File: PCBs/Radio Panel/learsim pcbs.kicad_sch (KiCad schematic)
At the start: 58 parts, among them SW1 MHz, SW2 KHz, SW3 2MD1T1B1M2QES-5, U1 ESP32-C6-DEV-KIT-N8, U2 MAX7219, U3 MAX7219

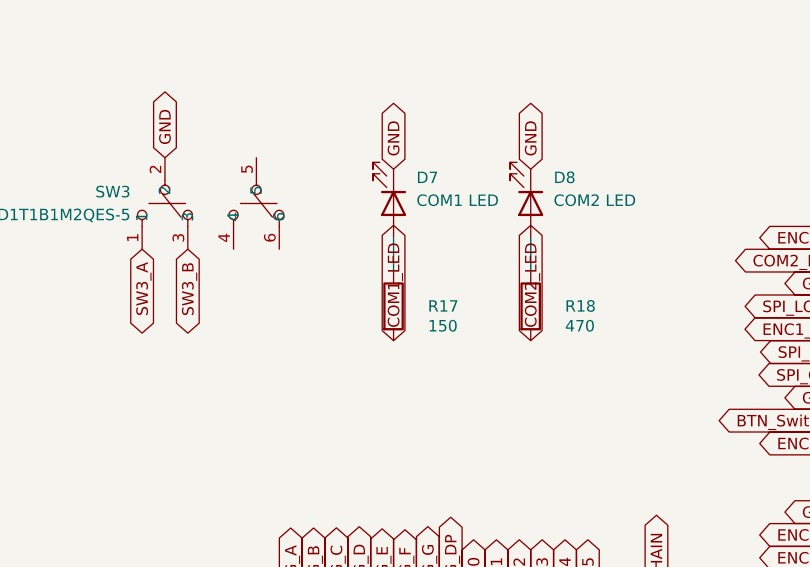
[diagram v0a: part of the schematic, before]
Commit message: Add new drill files and job configuration for learsim PCBs
- Created non-plated through hole (NPTH) drill file for learsim PCBs.
- Created plated through hole (PTH) drill file for learsim PCBs.
- Added job configuration file for learsim PCBs including specifications and file attributes.
- Updated symbol library table to include new components for the project.
- Modified project settings in .kicad_prl file to adjust active layer and visibility settings.
- Updated project properties in .kicad_pro file to include step file path and cleaned up used designators.
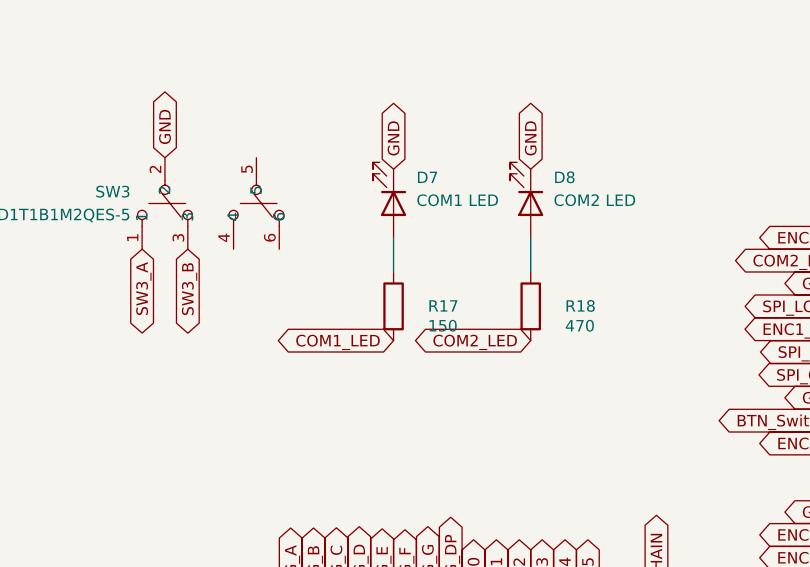
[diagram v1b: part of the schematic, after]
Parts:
- ADF1, COM1, COM2, NAV1, NAV2, Switch1: footprint PCM_Switch_Keyboard_Cherry_MX:SW_Cherry_MX_PCB -> PCM_Switch_Keyboard_Kailh:SW_Kailh_Choc_V2
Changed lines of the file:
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@@
 	(global_label "COM2_LED"
 		(shape bidirectional)
-		(at 76.2 92.71 90)
+		(at 76.2 92.71 180)
 		(fields_autoplaced yes)
 		(effects
@@
 				(size 1.27 1.27)
 			)
-			(justify left)
+			(justify right)
 		)
 		(property "Intersheetrefs" "${INTERSHEET_REFS}"
-			(at 84.2 92.71 0)
+			(at 62.4274 92.71 0)
 			(hide yes)
 			(show_name no)
@@
 					(size 1.27 1.27)
 				)
-				(justify left)
+				(justify right)
 			)
 		)
@@
 	(global_label "COM1_LED"
 		(shape bidirectional)
-		(at 60.96 92.71 90)
+		(at 60.96 92.71 180)
 		(fields_autoplaced yes)
 		(effects
@@
 				(size 1.27 1.27)
 			)
-			(justify left)
+			(justify right)
 		)
 		(property "Intersheetrefs" "${INTERSHEET_REFS}"
-			(at 68.96 92.71 0)
+			(at 47.1874 92.71 0)
 			(hide yes)
 			(show_name no)
@@
 					(size 1.27 1.27)
 				)
-				(justify left)
+				(justify right)
 			)
 		)
@@
 			)
 		)
-		(property "Footprint" "PCM_Switch_Keyboard_Cherry_MX:SW_Cherry_MX_PCB"
+		(property "Footprint" "PCM_Switch_Keyboard_Kailh:SW_Kailh_Choc_V2"
 			(at 161.29 52.07 0)
 			(hide yes)
@@
 			)
 		)
-		(property "Footprint" "PCM_Switch_Keyboard_Cherry_MX:SW_Cherry_MX_PCB"
+		(property "Footprint" "PCM_Switch_Keyboard_Kailh:SW_Kailh_Choc_V2"
 			(at 114.3 52.07 0)
 			(hide yes)
@@
 			)
 		)
-		(property "Footprint" "PCM_Switch_Keyboard_Cherry_MX:SW_Cherry_MX_PCB"
+		(property "Footprint" "PCM_Switch_Keyboard_Kailh:SW_Kailh_Choc_V2"
 			(at 144.78 52.07 0)
 			(hide yes)
@@
 			)
 		)
-		(property "Footprint" "PCM_Switch_Keyboard_Cherry_MX:SW_Cherry_MX_PCB"
+		(property "Footprint" "PCM_Switch_Keyboard_Kailh:SW_Kailh_Choc_V2"
 			(at 176.53 52.07 0)
 			(hide yes)
@@
 			)
 		)
-		(property "Footprint" "PCM_Switch_Keyboard_Cherry_MX:SW_Cherry_MX_PCB"
+		(property "Footprint" "PCM_Switch_Keyboard_Kailh:SW_Kailh_Choc_V2"
 			(at 191.77 52.07 0)
 			(hide yes)
@@
 			)
 		)
-		(property "Footprint" "PCM_Switch_Keyboard_Cherry_MX:SW_Cherry_MX_PCB"
+		(property "Footprint" "PCM_Switch_Keyboard_Kailh:SW_Kailh_Choc_V2"
 			(at 130.81 52.07 0)
 			(hide yes)

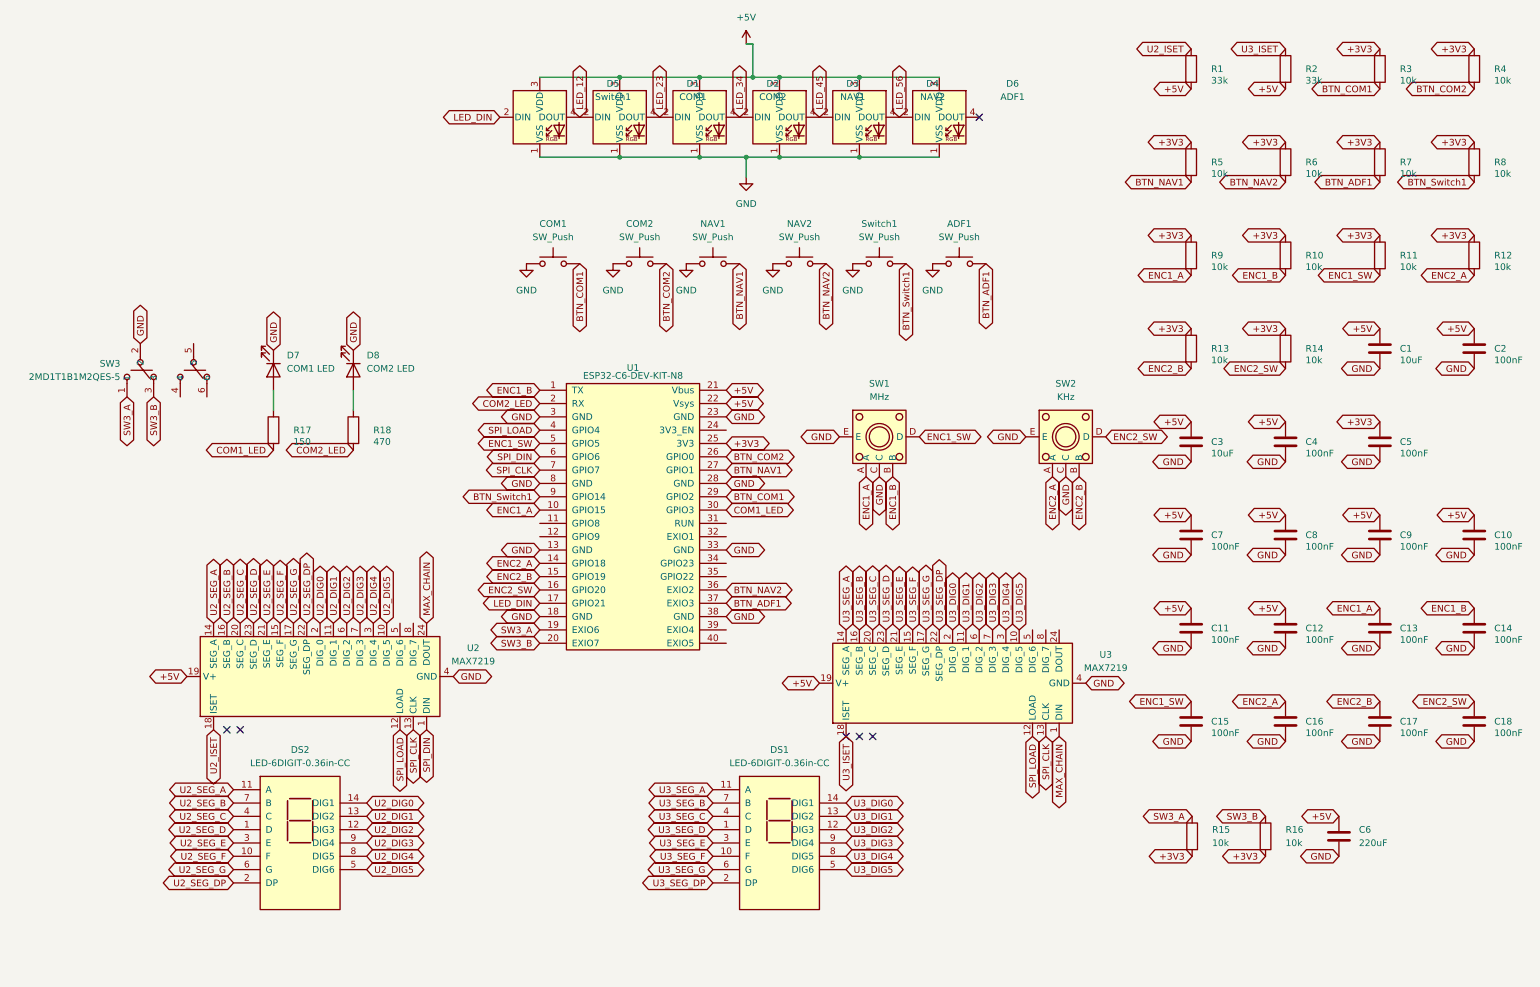
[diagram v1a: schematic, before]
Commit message: Update drill files and job configuration for radio panel PCBs
- Updated creation dates in NPTH and PTH drill files to 2026-08-13.
- Modified drill sizes for various tool definitions in NPTH and PTH files.
- Added new coordinates for tool paths in PTH drill file.
- Adjusted job configuration file creation date to 2026-08-13.
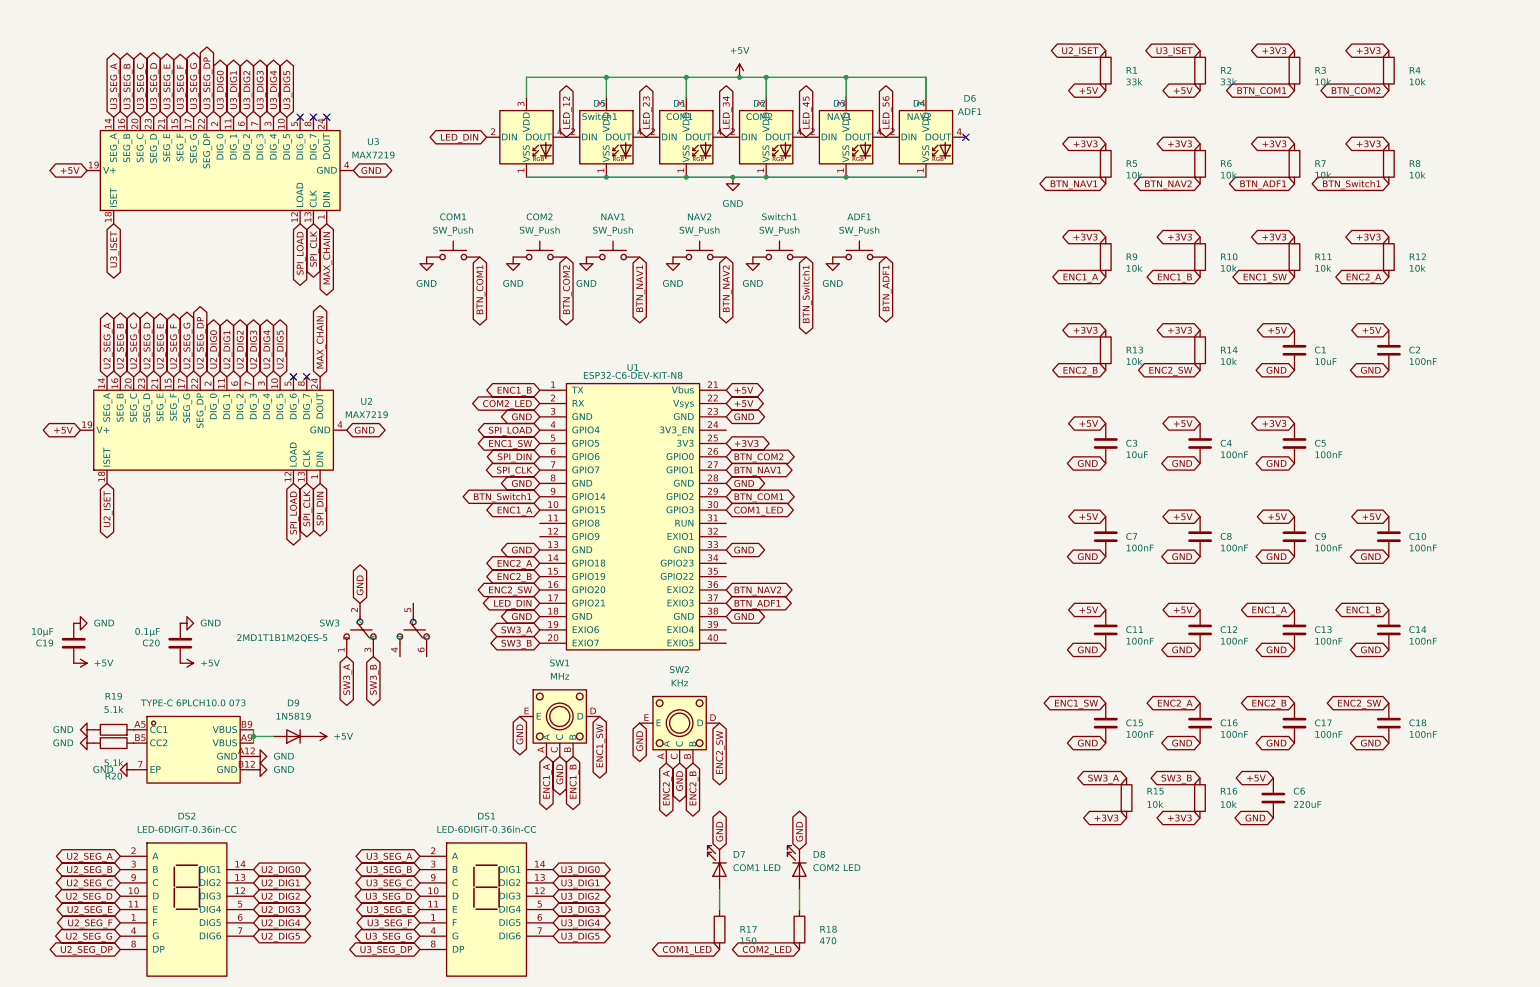
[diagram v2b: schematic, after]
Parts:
- added C19: 10µF, Capacitor_THT:C_Disc_D5.0mm_W2.5mm_P5.00mm, symbol Device:C
- added C20: 0.1µF, Capacitor_THT:C_Disc_D5.0mm_W2.5mm_P5.00mm, symbol Device:C
- added D9: 1N5819, Diode_THT:D_DO-41_SOD81_P7.62mm_Horizontal, symbol Device:D
- added R19, R20: 5.1k, Resistor_THT:R_Axial_DIN0207_L6.3mm_D2.5mm_P7.62mm_Horizontal, symbol Device:R
- added U4: TYPE-C 6PLCH10.0 073, Rotary:USB-C-TH_TYPE-C-6PLCH10.0-073, symbol Rotary:TYPE-C6PLCH10.0073
- DS1, DS2: footprint 7-Segment Display:LED-6DIGIT-0.36in-CC_14P -> LED-6DIGIT-0.36in-CC_14P:LED-6DIGIT-0.36in-CC_14P
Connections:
- net +5V: now also C19.1, C20.1, D9.1 (K)
- net GND: now also C19.2, C20.2, R19.1, R20.2, U4.7 (EP), U4.A12 (GND), U4.B12 (GND)
- net U2_DIG3: now also DS2.5 (DIG4); no longer DS2.9 (DIG4)
- net U2_DIG4: now also DS2.6 (DIG5); no longer DS2.8 (DIG5)
- net U2_DIG5: now also DS2.7 (DIG6); no longer DS2.5 (DIG6)
- net U2_SEG_A: now also DS2.2 (A); no longer DS2.11 (A)
- net U2_SEG_B: now also DS2.3 (B); no longer DS2.7 (B)
- net U2_SEG_C: now also DS2.9 (C); no longer DS2.4 (C)
- net U2_SEG_D: now also DS2.10 (D); no longer DS2.1 (D)
- net U2_SEG_DP: now also DS2.8 (DP); no longer DS2.2 (DP)
- net U2_SEG_E: now also DS2.11 (E); no longer DS2.3 (E)
- net U2_SEG_F: now also DS2.1 (F); no longer DS2.10 (F)
- net U2_SEG_G: now also DS2.4 (G); no longer DS2.6 (G)
- net U3_DIG3: now also DS1.5 (DIG4); no longer DS1.9 (DIG4)
- net U3_DIG4: now also DS1.6 (DIG5); no longer DS1.8 (DIG5)
- net U3_DIG5: now also DS1.7 (DIG6); no longer DS1.5 (DIG6)
- net U3_SEG_A: now also DS1.2 (A); no longer DS1.11 (A)
- net U3_SEG_B: now also DS1.3 (B); no longer DS1.7 (B)
- net U3_SEG_C: now also DS1.9 (C); no longer DS1.4 (C)
- net U3_SEG_D: now also DS1.10 (D); no longer DS1.1 (D)
- net U3_SEG_DP: now also DS1.8 (DP); no longer DS1.2 (DP)
- net U3_SEG_E: now also DS1.11 (E); no longer DS1.3 (E)
- net U3_SEG_F: now also DS1.1 (F); no longer DS1.10 (F)
- net U3_SEG_G: now also DS1.4 (G); no longer DS1.6 (G)
- new net: R20.1, U4.B5 (CC2)
- new net: R19.2, U4.A5 (CC1)
- new net: D9.2 (A), U4.A9 (VBUS), U4.B9 (VBUS)
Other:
- company: (none) -> Learsim
- title: (none) -> Learsim Radio Panel
- moved on the sheet: ADF1, C1, C10, C11, C12, C13, C14, C15, C16, C17, C18, C2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
